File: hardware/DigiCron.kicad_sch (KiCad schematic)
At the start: 18 parts, among them J100 Solder pad, J101 Solder pad, J102 Solder pad, J103 Solder pad, Q100 BSS138, Q101 AO3400A, U100 MDBT50Q-U1MV2, U101 HCMS-3917, U102 HCMS-3917, U103 LTR-390UV-01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

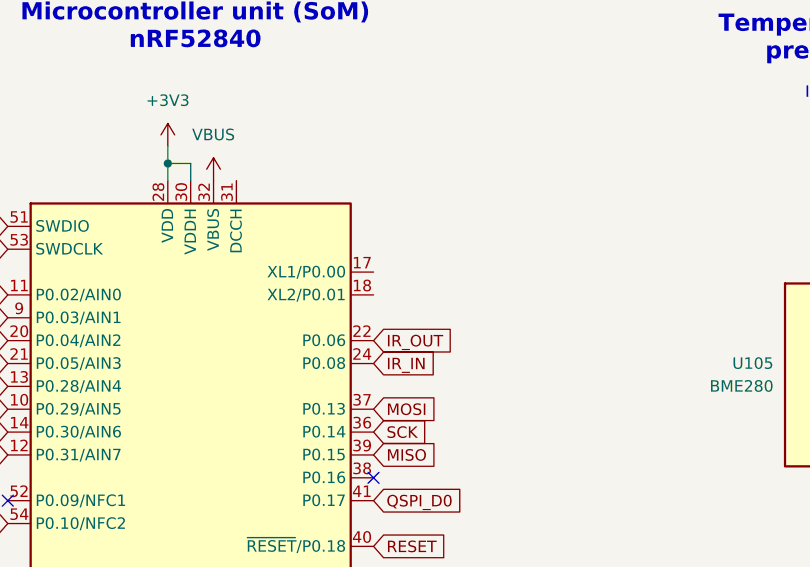
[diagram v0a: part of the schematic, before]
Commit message: Add crystal oscillator and hide designators from PCB
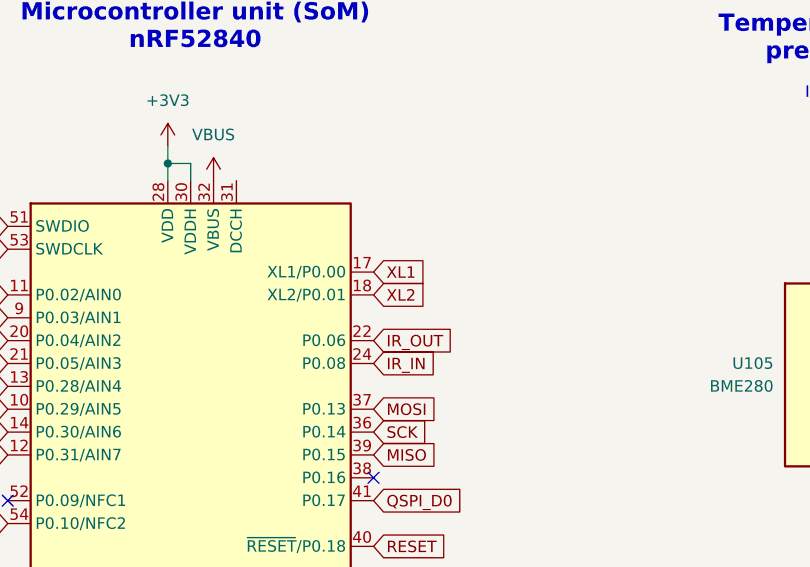
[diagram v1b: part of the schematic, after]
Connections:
- net XL1: now reaches U100.17 (XL1/P0.00)
- net XL2: now reaches U100.18 (XL2/P0.01)
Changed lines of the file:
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@@
+		)
+	)
+	(global_label "XL1"
+		(shape input)
+		(at 81.28 50.8 0)
+		(fields_autoplaced yes)
+		(effects
+			(font
+				(size 1.27 1.27)
+			)
+			(justify left)
+		)
+		(property "Intersheetrefs" "${INTERSHEET_REFS}"
+			(at 87.7123 50.8 0)
+			(effects
+				(font
+					(size 1.27 1.27)
+				)
+				(justify left)
+				(hide yes)
+			)
 		)
 	)
@@
 				(hide yes)
 			)
+		)
+	)
+	(global_label "XL2"
+		(shape input)
+		(at 81.28 53.34 0)
+		(fields_autoplaced yes)
+		(effects
+			(font
+				(size 1.27 1.27)
+			)
+			(justify left)
+		)
+		(property "Intersheetrefs" "${INTERSHEET_REFS}"
+			(at 87.7123 53.34 0)
+			(effects
+				(font
+					(size 1.27 1.27)
+				)
+				(justify left)
+				(hide yes)
+			)

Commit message: Perform PCB routing (WIP)
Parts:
- removed U103: LTR-390UV-01, LTR390:SMD6_LTR-390UV-01_LTO, symbol 2024-12-11_22-26-57:LTR-390UV-01
- added R104: 10K, Capacitor_SMD:C_0201_0603Metric_Pad0.64x0.40mm_HandSolder, symbol Device:R
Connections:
- net A2 is gone; now on net SCL: U100.14 (P0.30/AIN6)
- net AREF is gone; now on net 5V_EN: U100.12 (P0.31/AIN7)
- net +3V3: now also U105.2 (CSB), U105.5 (SDO); no longer U104.12 (SDO/ALTADDRESS)
- net 5V_EN: no longer U100.4 (P1.11)
- net GND: now also U104.12 (SDO/ALTADDRESS), R104.1
- net SCL: no longer U100.27 (TRACEDATA2/P0.11)
- net SDA: now also U100.10 (P0.29/AIN5); no longer U100.29 (TRACEDATA1/P0.12)
- net VDIV: now also U100.16 (P0.27); no longer U100.10 (P0.29/AIN5)
- net at Q101.1 (G), R103.2: now also R104.2
- net A1: no longer names the net of U100.21 (P0.05/AIN3)
- net A3: no longer names the net of U100.13 (P0.28/AIN4)
- net ADPS_IRQ: no longer names the net of U100.47 (TRACEDATA0/P1.00)
- net IR_IN: no longer names the net of U100.24 (P0.08)
- net MISO: no longer names the net of U100.39 (P0.15)
- net MOSI: no longer names the net of U100.37 (P0.13)
- net QSPI_D0: no longer names the net of U100.41 (P0.17)
- net QSPI_D1: no longer names the net of U100.46 (P0.22)
- net QSPI_D2: no longer names the net of U100.45 (P0.23)
- net QSPI_D3: no longer names the net of U100.43 (P0.21)
- net QSPI_SCK: no longer names the net of U100.42 (P0.19)
- net RXD: no longer names the net of U100.48 (P0.24)
- net SCK: no longer names the net of U100.36 (P0.14)
- net TXD: no longer names the net of U100.49 (P0.25)
- no-connect marks 14 -> 29
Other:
- note removed: "I²C address: 0x1D (alt)"
- note removed: "UV and visible light sensor"
- moved on the sheet: D101, J100, J101, Q101, R103, U102

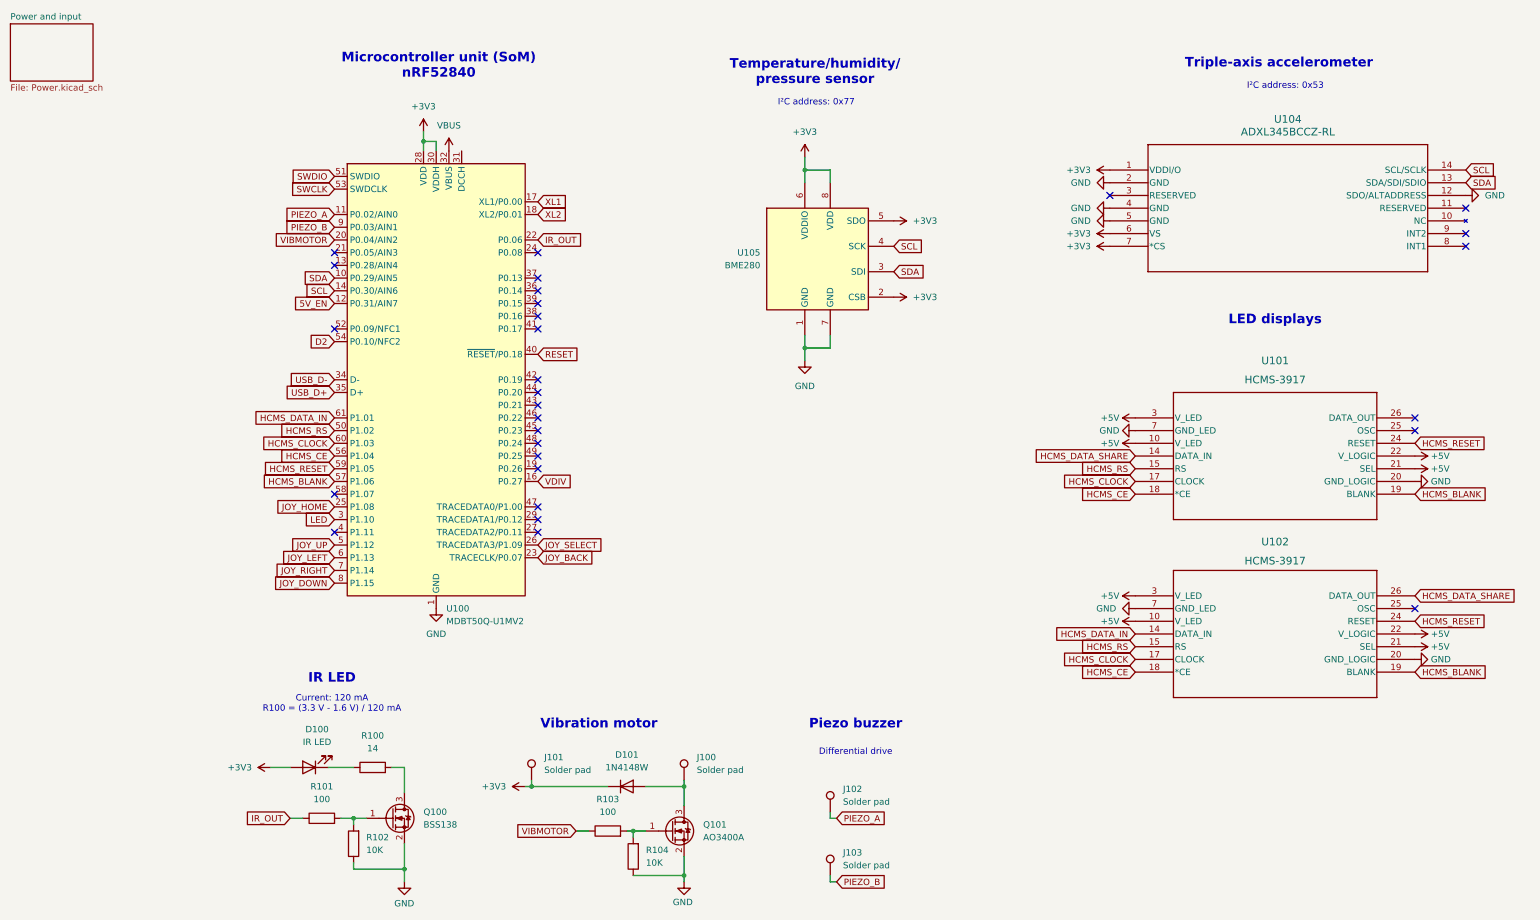
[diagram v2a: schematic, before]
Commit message: Check over PCB design and re-add LTR390
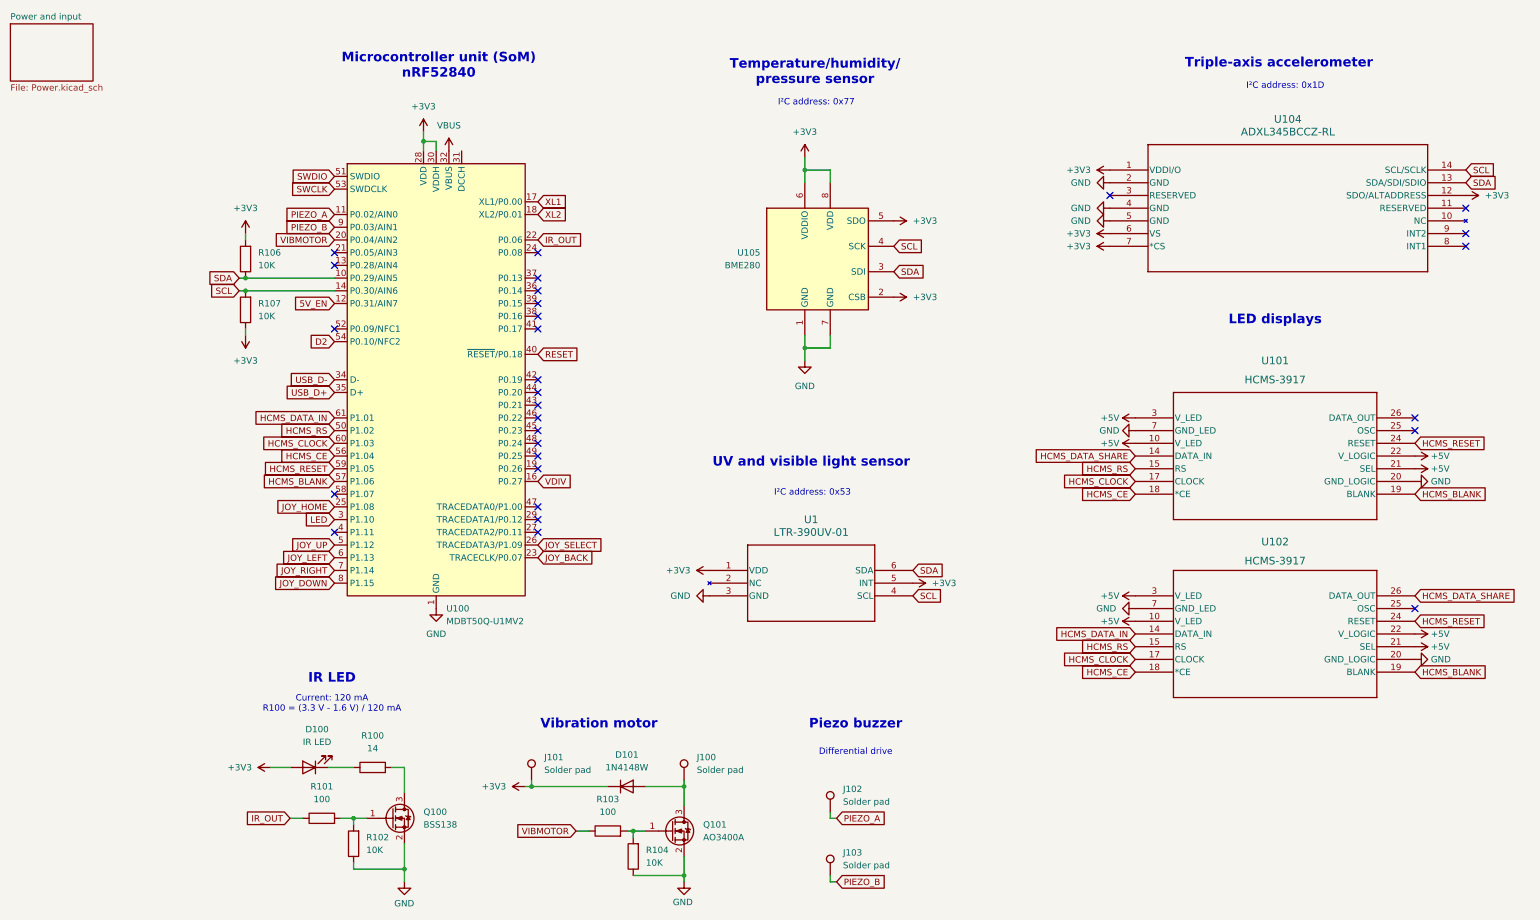
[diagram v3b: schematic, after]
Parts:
- added R106, R107: 10K, Capacitor_SMD:C_0201_0603Metric_Pad0.64x0.40mm_HandSolder, symbol Device:R
- added U1: LTR-390UV-01, SMD6_LTR-390UV-01_LTO, symbol LTR390:LTR-390UV-01
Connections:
- net +3V3: now also U104.12 (SDO/ALTADDRESS), R106.2, R107.1, U1.1 (VDD), U1.5 (INT)
- net GND: now also U1.3 (GND); no longer U104.12 (SDO/ALTADDRESS)
- net SCL: now also R107.2, U1.4 (SCL)
- net SDA: now also R106.1, U1.6 (SDA)
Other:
- note added: "I²C address: 0x1D"
- note added: "UV and visible light sensor"

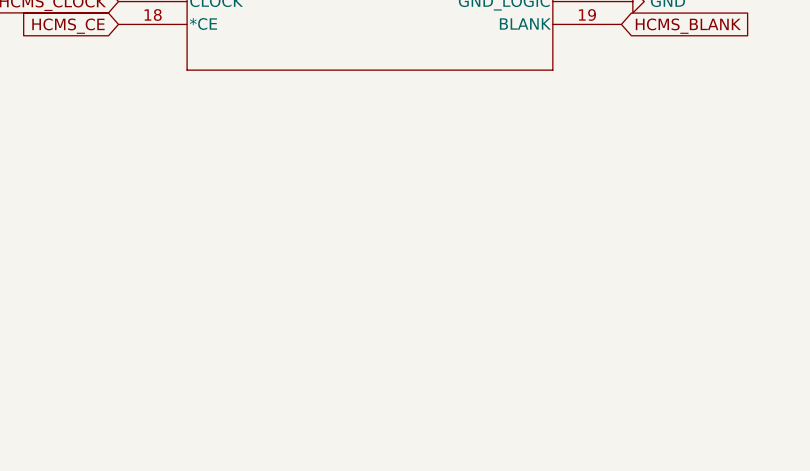
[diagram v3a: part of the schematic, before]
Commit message: Add mounting tabs to edges of PCB
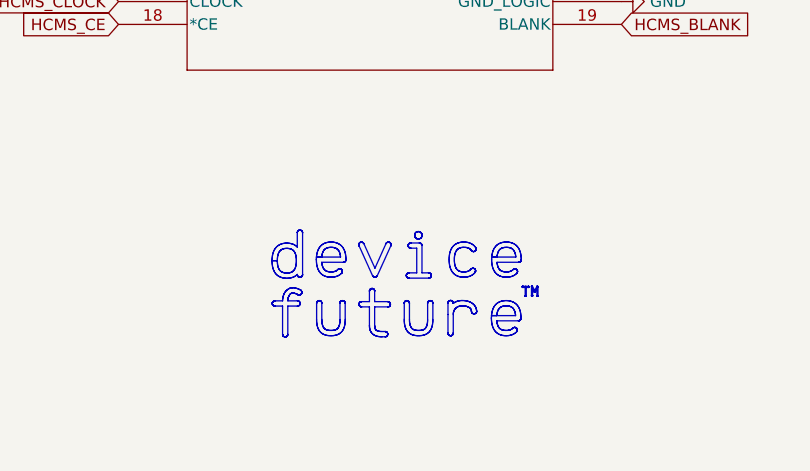
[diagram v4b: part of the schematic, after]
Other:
- company: (none) -> DeviceFuture
- title: (none) -> DigiCron

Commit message: Update PCB to use 0402 resistor/capacitor packages
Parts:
- R100, R101, R102, R103, R104, R106, R107: footprint Capacitor_SMD:C_0201_0603Metric_Pad0.64x0.40mm_HandSolder -> Resistor_SMD:R_0402_1005Metric_Pad0.72x0.64mm_HandSolder
- U1: footprint SMD6_LTR-390UV-01_LTO -> LTR390:SMD6_LTR-390UV-01_LTO
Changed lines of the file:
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@@
 			)
 		)
-		(property "Footprint" "Capacitor_SMD:C_0201_0603Metric_Pad0.64x0.40mm_HandSolder"
+		(property "Footprint" "Resistor_SMD:R_0402_1005Metric_Pad0.72x0.64mm_HandSolder"
 			(at 38.1 175.768 90)
 			(effects
@@
 			)
 		)
-		(property "Footprint" "Capacitor_SMD:C_0201_0603Metric_Pad0.64x0.40mm_HandSolder"
+		(property "Footprint" "Resistor_SMD:R_0402_1005Metric_Pad0.72x0.64mm_HandSolder"
 			(at 102.108 181.61 90)
 			(effects
@@
 			)
 		)
-		(property "Footprint" "Capacitor_SMD:C_0201_0603Metric_Pad0.64x0.40mm_HandSolder"
+		(property "Footprint" "Resistor_SMD:R_0402_1005Metric_Pad0.72x0.64mm_HandSolder"
 			(at 46.228 179.07 90)
 			(effects
@@
 			)
 		)
-		(property "Footprint" "Capacitor_SMD:C_0201_0603Metric_Pad0.64x0.40mm_HandSolder"
+		(property "Footprint" "Resistor_SMD:R_0402_1005Metric_Pad0.72x0.64mm_HandSolder"
 			(at 24.638 62.23 90)
 			(effects
@@
 			)
 		)
-		(property "Footprint" "SMD6_LTR-390UV-01_LTO"
+		(property "Footprint" "LTR390:SMD6_LTR-390UV-01_LTO"
 			(at 115.57 124.46 0)
 			(effects
@@
 			)
 		)
-		(property "Footprint" "Capacitor_SMD:C_0201_0603Metric_Pad0.64x0.40mm_HandSolder"
+		(property "Footprint" "Resistor_SMD:R_0402_1005Metric_Pad0.72x0.64mm_HandSolder"
 			(at 95.25 178.308 90)
 			(effects
@@
 			)
 		)
-		(property "Footprint" "Capacitor_SMD:C_0201_0603Metric_Pad0.64x0.40mm_HandSolder"
+		(property "Footprint" "Resistor_SMD:R_0402_1005Metric_Pad0.72x0.64mm_HandSolder"
 			(at 48.26 165.608 90)
 			(effects
@@
 			)
 		)
-		(property "Footprint" "Capacitor_SMD:C_0201_0603Metric_Pad0.64x0.40mm_HandSolder"
+		(property "Footprint" "Resistor_SMD:R_0402_1005Metric_Pad0.72x0.64mm_HandSolder"
 			(at 24.638 72.39 90)
 			(effects

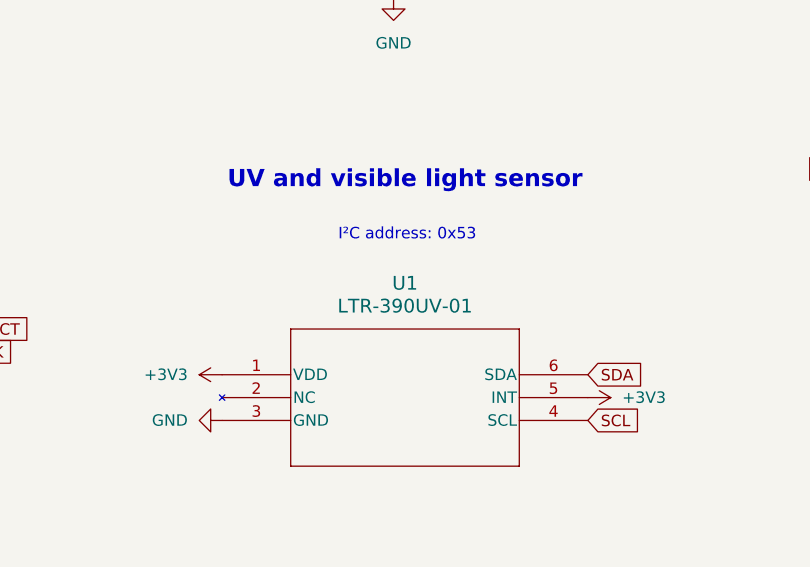
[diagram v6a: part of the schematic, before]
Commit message: Make a few changes to footprint selection and resistor/capacitor values
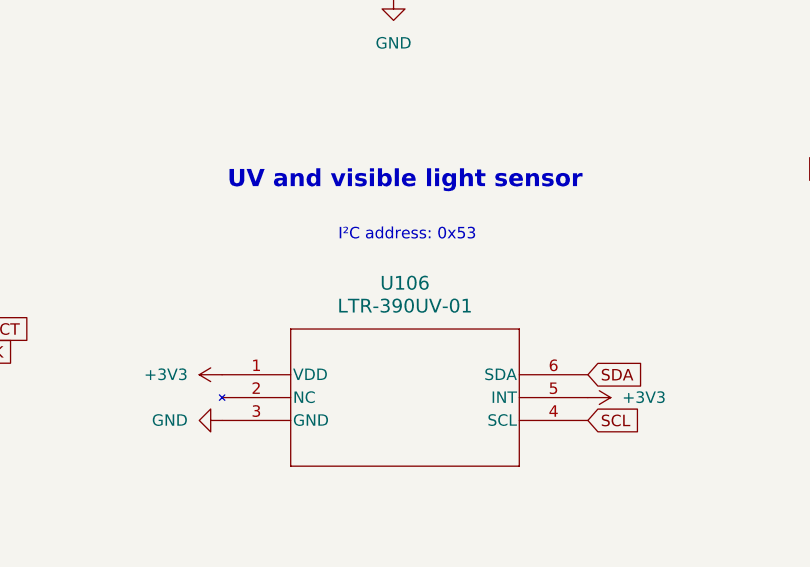
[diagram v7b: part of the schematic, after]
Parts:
- renumbered U1 to U106
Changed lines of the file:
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@@
 		(dnp no)
 		(fields_autoplaced yes)
-		(property "Reference" "U1"
+		(property "Reference" "U106"
 			(at 135.89 114.3 0)
 			(effects
@@
 			(project ""
 				(path "/da54d175-8762-4f8c-be46-30694592bf7b"
-					(reference "U1")
+					(reference "U106")
 					(unit 1)
 				)

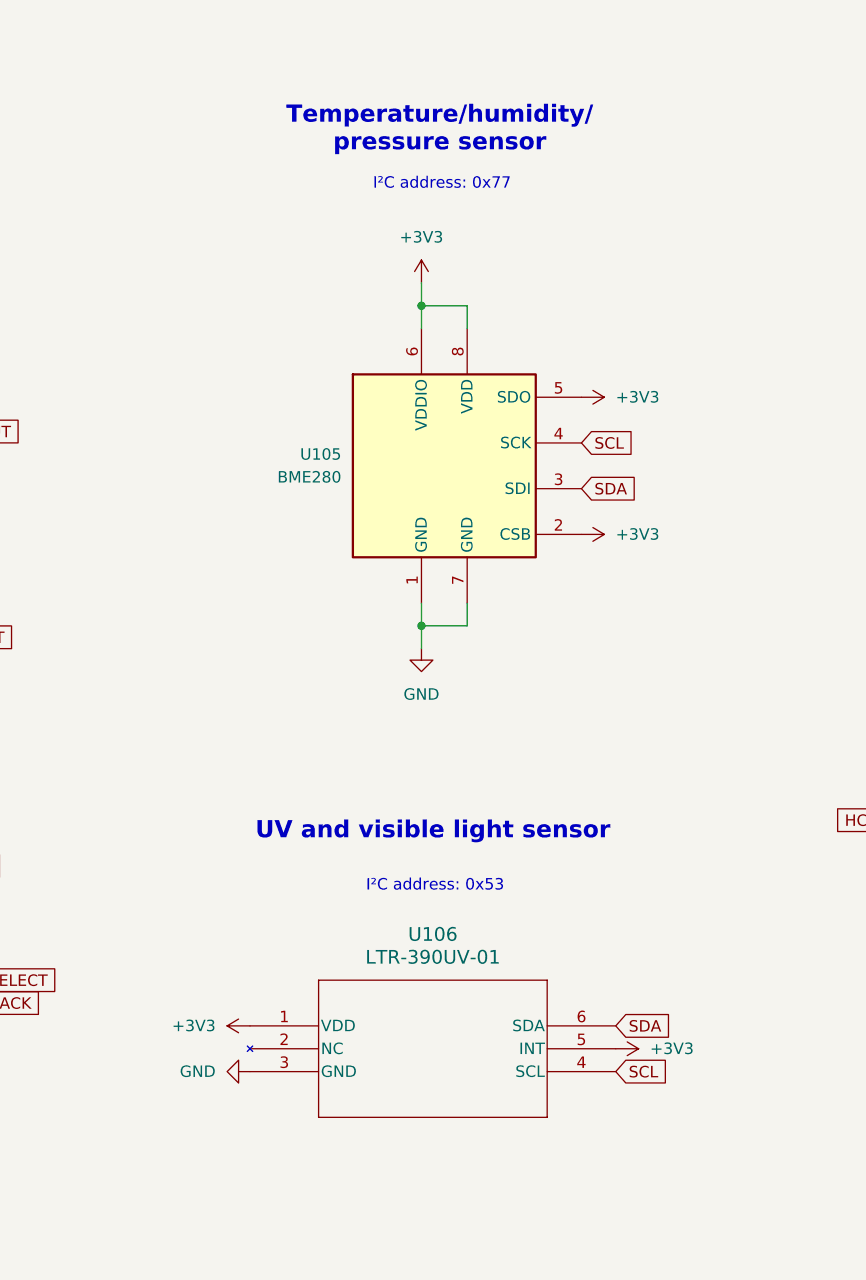
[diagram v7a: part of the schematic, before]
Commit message: Remove LTR-390 to make assembly easier
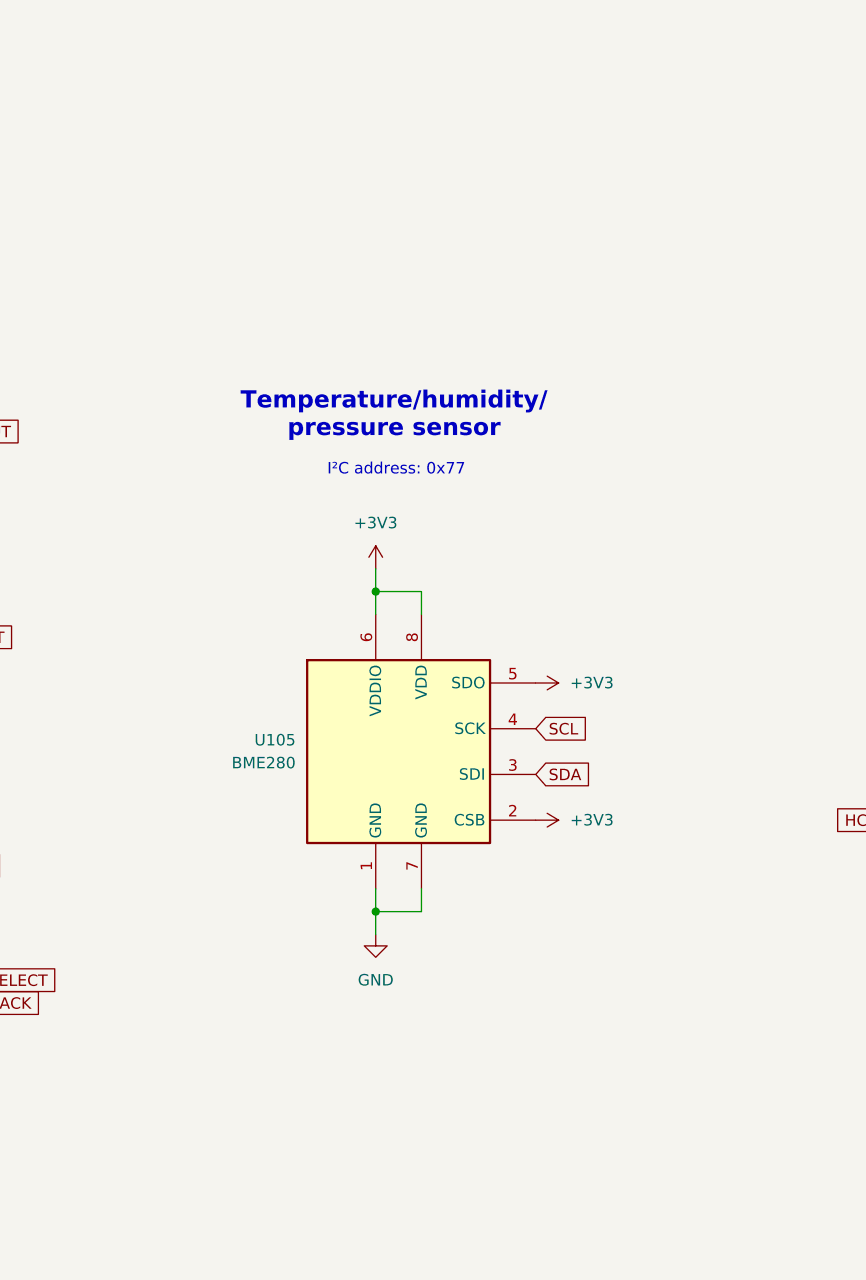
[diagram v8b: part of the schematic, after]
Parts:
- removed U106: LTR-390UV-01, LTR390:SMD6_LTR-390UV-01_LTO, symbol LTR390:LTR-390UV-01
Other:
- note removed: "I²C address: 0x53"
- note removed: "UV and visible light sensor"
- moved on the sheet: U105
